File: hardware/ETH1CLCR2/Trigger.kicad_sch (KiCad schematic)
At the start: 22 parts, among them U301 74AC125, U302 TXB0104PW, U303 ADuM5402

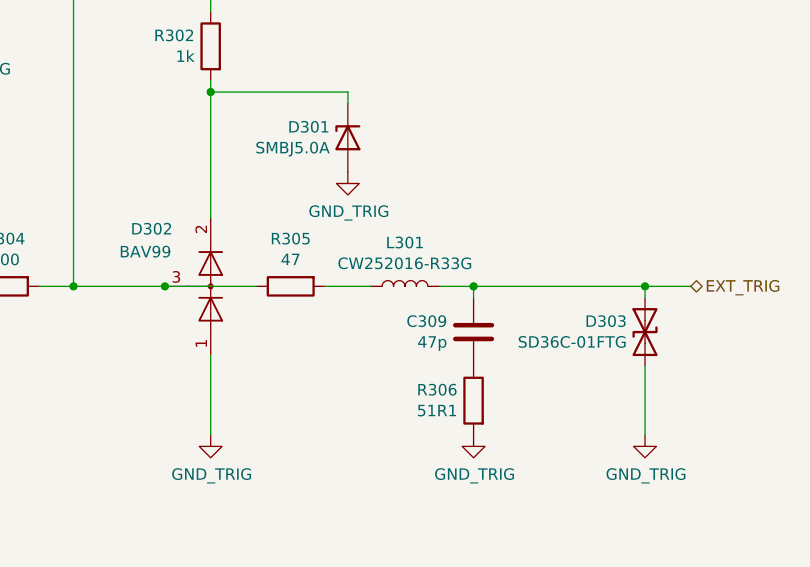
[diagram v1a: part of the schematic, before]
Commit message: Converted HW files to KiCAD 7.0.
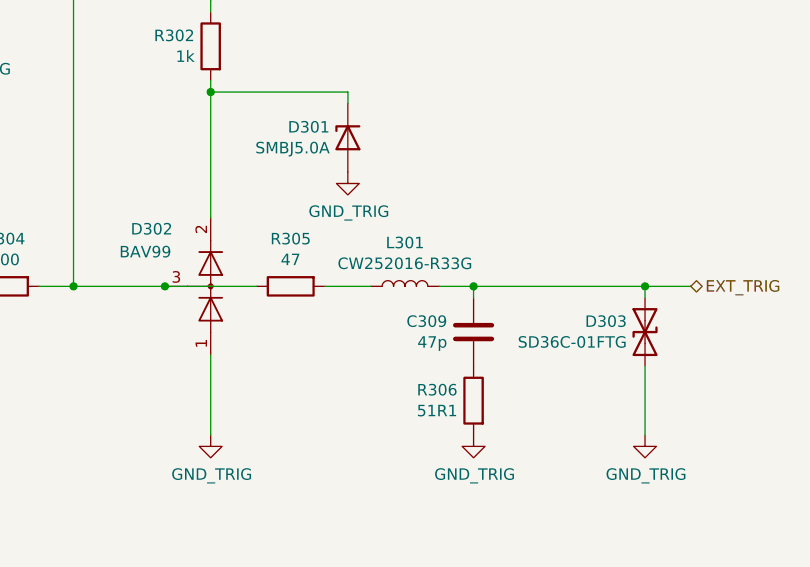
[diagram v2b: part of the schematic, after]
